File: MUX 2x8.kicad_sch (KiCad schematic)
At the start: 2 parts, among them U1408 74LS257, U1409 74LS257

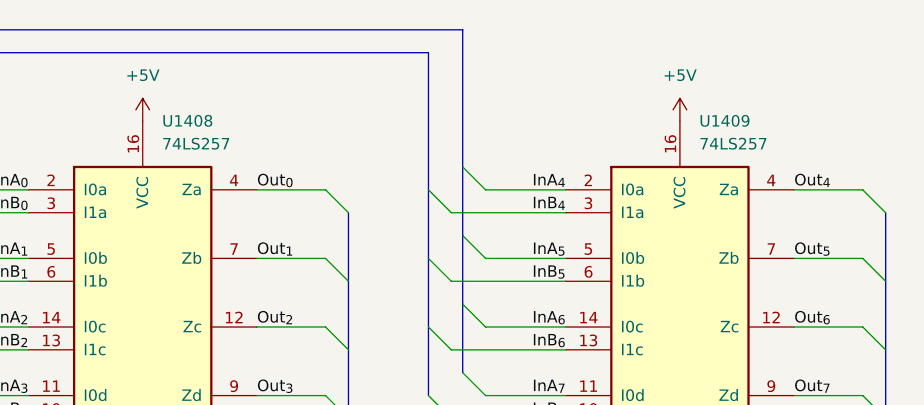
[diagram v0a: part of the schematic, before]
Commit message: More cleanup and preparing signals for control logic
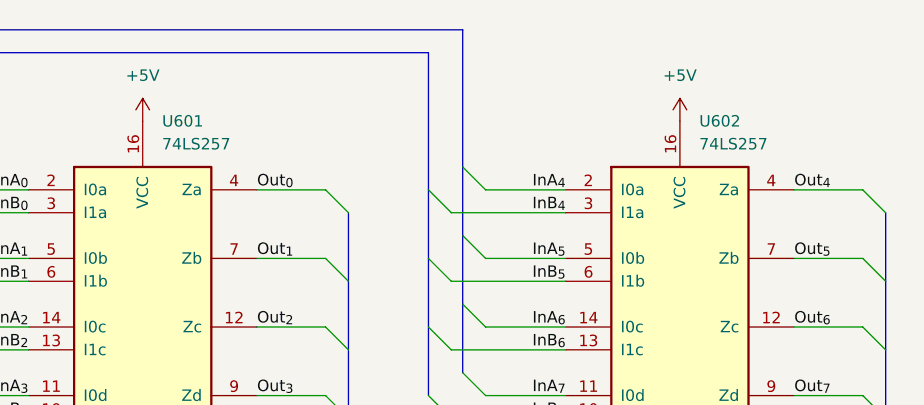
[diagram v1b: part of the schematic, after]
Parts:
- renumbered U1408 to U601, U1409 to U602
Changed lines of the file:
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@@
 		(dnp no)
 		(fields_autoplaced yes)
-		(property "Reference" "#PWR01417"
+		(property "Reference" "#PWR0602"
 			(at 85.09 92.71 0)
 			(effects
@@
 			(project "BRISC8"
 				(path "/e198223b-f7bd-4b26-ae2e-259db8d07fb6/d081cdcb-1181-4657-9580-dc3ba9a85775/5793eec4-481b-48e8-b2cb-f88bcf76a93f"
-					(reference "#PWR01417")
+					(reference "#PWR0602")
 					(unit 1)
 				)
@@
 		(dnp no)
 		(fields_autoplaced yes)
-		(property "Reference" "#PWR01416"
+		(property "Reference" "#PWR0603"
 			(at 144.78 41.91 0)
 			(effects
@@
 			(project "BRISC8"
 				(path "/e198223b-f7bd-4b26-ae2e-259db8d07fb6/d081cdcb-1181-4657-9580-dc3ba9a85775/5793eec4-481b-48e8-b2cb-f88bcf76a93f"
-					(reference "#PWR01416")
+					(reference "#PWR0603")
 					(unit 1)
 				)
@@
 		(dnp no)
 		(fields_autoplaced yes)
-		(property "Reference" "U1409"
+		(property "Reference" "U602"
 			(at 146.9233 38.1 0)
 			(effects
@@
 			(project "BRISC8"
 				(path "/e198223b-f7bd-4b26-ae2e-259db8d07fb6/d081cdcb-1181-4657-9580-dc3ba9a85775/5793eec4-481b-48e8-b2cb-f88bcf76a93f"
-					(reference "U1409")
+					(reference "U602")
 					(unit 1)
 				)
@@
 		(dnp no)
 		(fields_autoplaced yes)
-		(property "Reference" "U1408"
+		(property "Reference" "U601"
 			(at 87.2333 38.1 0)
 			(effects
@@
 			(project "BRISC8"
 				(path "/e198223b-f7bd-4b26-ae2e-259db8d07fb6/d081cdcb-1181-4657-9580-dc3ba9a85775/5793eec4-481b-48e8-b2cb-f88bcf76a93f"
-					(reference "U1408")
+					(reference "U601")
 					(unit 1)
 				)
@@
 		(dnp no)
 		(fields_autoplaced yes)
-		(property "Reference" "#PWR01415"
+		(property "Reference" "#PWR0601"
 			(at 85.09 41.91 0)
 			(effects
@@
 			(project "BRISC8"
 				(path "/e198223b-f7bd-4b26-ae2e-259db8d07fb6/d081cdcb-1181-4657-9580-dc3ba9a85775/5793eec4-481b-48e8-b2cb-f88bcf76a93f"
-					(reference "#PWR01415")
+					(reference "#PWR0601")
 					(unit 1)
 				)
@@
 		(dnp no)
 		(fields_autoplaced yes)
-		(property "Reference" "#PWR01418"
+		(property "Reference" "#PWR0604"
 			(at 144.78 92.71 0)
 			(effects
@@
 			(project "BRISC8"
 				(path "/e198223b-f7bd-4b26-ae2e-259db8d07fb6/d081cdcb-1181-4657-9580-dc3ba9a85775/5793eec4-481b-48e8-b2cb-f88bcf76a93f"
-					(reference "#PWR01418")
-					(unit 1)
-				)
+					(reference "#PWR0604")
+					(unit 1)
+				)

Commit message: Draft Schematic
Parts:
- added C601, C602: 0.1uF, Capacitor_THT:C_Rect_L4.0mm_W2.5mm_P2.50mm, symbol Device:C
- U601, U602: value 74LS257 -> 74HC257; footprint (none) -> Package_DIP:DIP-16_W7.62mm
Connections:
- net +5V: now also C601.1, C602.1
- net GND: now also C601.2, C602.2
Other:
- company: (none) -> Brian Duffy
- title: (none) -> BRISC8 CPU
